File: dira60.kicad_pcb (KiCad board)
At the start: 2 copper layers, 285 x 94.5 mm, 201 parts, among them U0 ATmega32U4-AU, X0 XTAL_GND

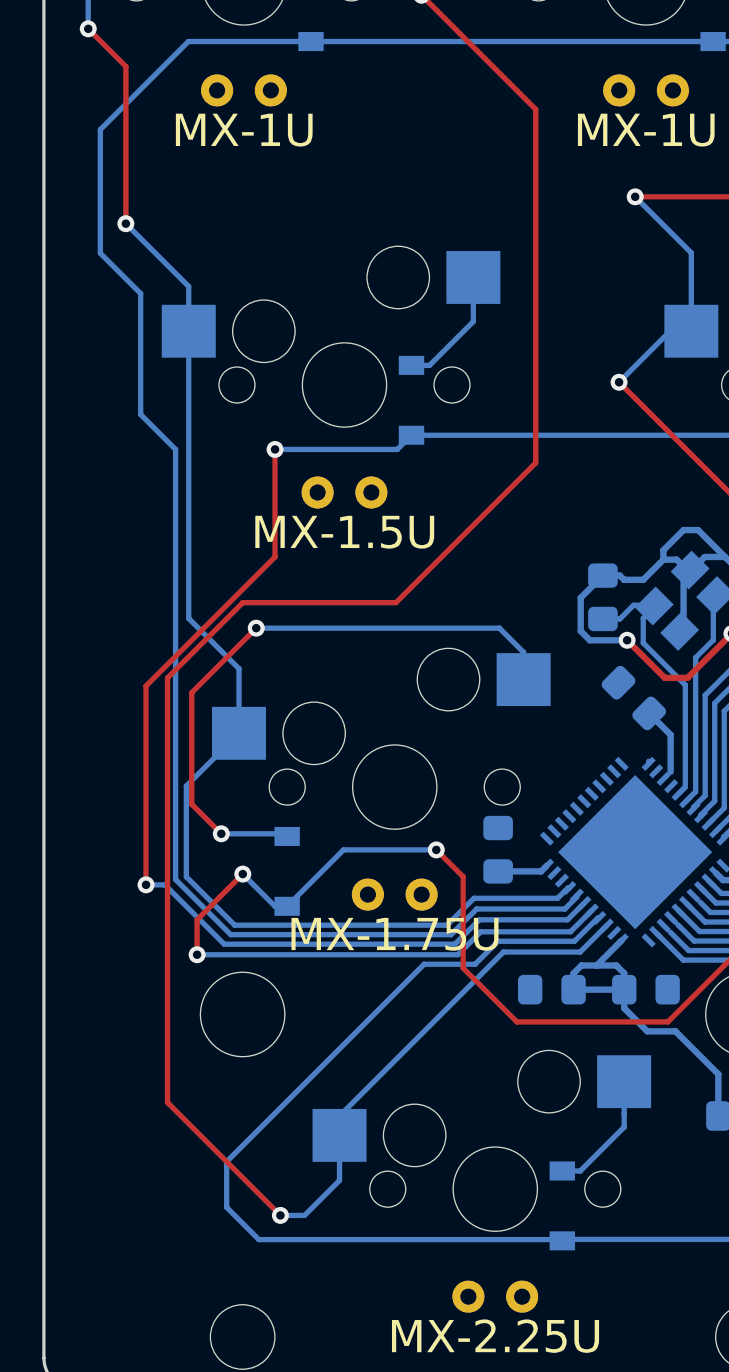
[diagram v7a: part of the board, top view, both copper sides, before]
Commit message: Routed all rows & cols
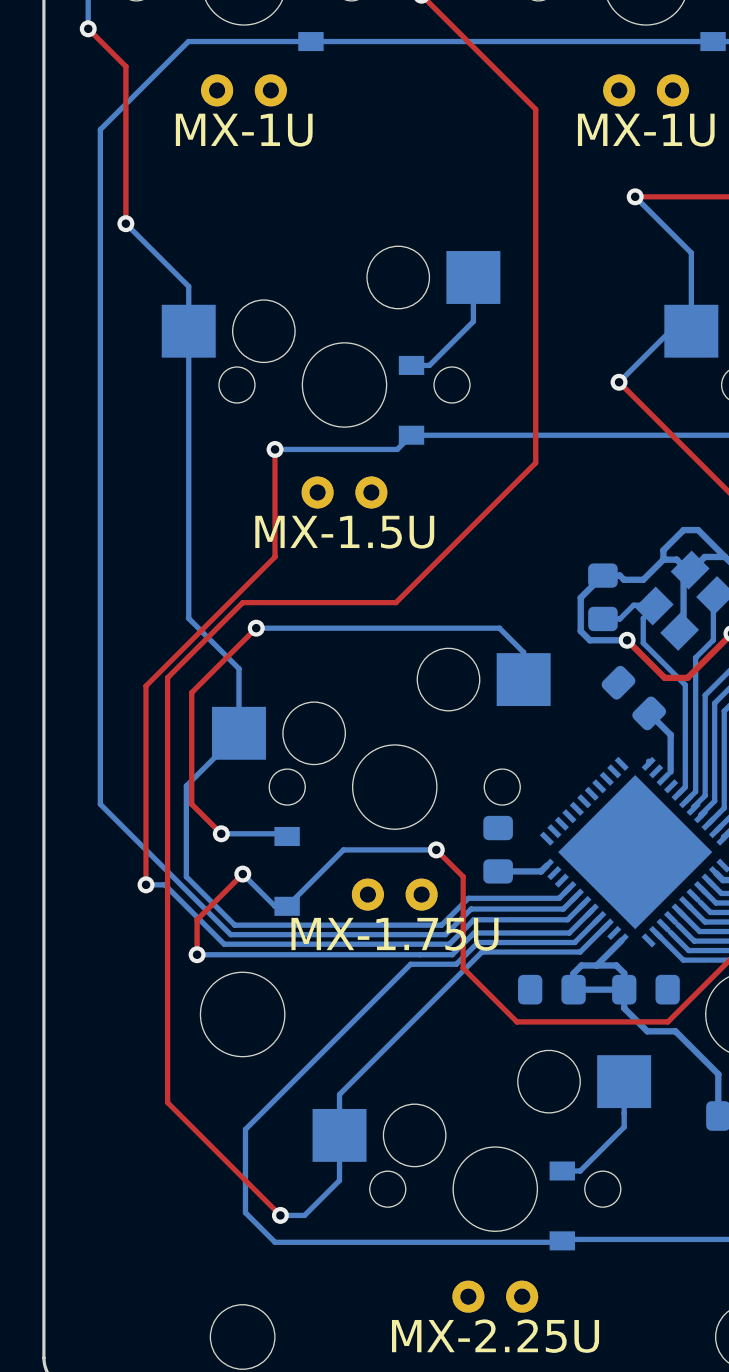
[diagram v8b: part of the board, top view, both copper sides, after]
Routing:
- net ROW3: track 295.2 -> 294.6 mm
- net COL1: track 101.0 -> 101.6 mm
